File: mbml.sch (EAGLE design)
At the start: 16 parts, among them IC1 MAX392CPE, J1 CON-2B2B-XH-A(LF)(SN), J2 CON-2B2B-XH-A(LF)(SN), K1 G5SB, Q1 2N2222, X1 43160-1102

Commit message: Finished board
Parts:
- removed IC1: MAX392CPE, maxim:MAX392CPE
- removed J1, J2, U$2, U$3, U$4: CON-2B2B-XH-A(LF)(SN), FVP:CON-2B2B-XH-A(LF)(SN)
- removed U$5: CON-2, FVP:CON-2
- added OK1: ILQ1, optocoupler:ILQ1
- added R1, R2, R3, R6: 470, resistor:R-US_0204/5
- added R4, R5: 10k, resistor:R-US_0204/5
- added X2: CON-2, FVP:CON-2
- added X3, X4, X5, X6, X7, X8: CON-2B2B-XH-A(LF)(SN), FVP:CON-2B2B-XH-A(LF)(SN)
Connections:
- new net N$15: OK1A.COL, X7.1
- new net N$16: OK1A.EMIT, X7.2
- new net N$17: OK1D.A, R6.1
- new net N$18: R6.2, U$1.D9
- new net N$19: OK1D.COL, X8.1
- new net N$20: OK1D.EMIT, X8.2
- new net N$7: OK1B.A, R2.1
- net GND: now also OK1A.C, OK1B.C, OK1C.C, OK1D.C, R4.2, R5.2, X2.1, X3.1, X4.1; no longer J1.1, J2.1, U$5.1
- net MON_PWR: now also X2.2; no longer U$5.2
- net N$1: now also R4.1, X4.2; no longer J2.2
- net N$10: now also R3.2; no longer IC1.IN1
- net N$11: now also OK1C.COL, X5.1; no longer IC1.NO3, U$4.2
- net N$12: now also OK1C.EMIT, X5.2; no longer IC1.COM3, U$4.1
- net N$13: now also OK1B.COL, X6.1; no longer IC1.COM2, U$3.1
- net N$14: now also OK1B.EMIT, X6.2; no longer IC1.COM1, U$2.1
- net N$2: now also R5.1, X3.2; no longer J1.2
- net N$4: now also R1.2; no longer IC1.IN3
- net N$5: now also U$1.D10; no longer U$1.D9
- net N$6: now also OK1C.A, R3.1; no longer IC1.NO1, U$2.2
- net N$8: now also OK1A.A, R1.1; no longer IC1.NO2, U$3.2
- net N$9: now also R2.2; no longer IC1.IN2
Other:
- note added: "1.0.0"
- note added: "9-23-16"
- note added: "A"
- note added: "AUX"
- note added: "CLIENT:"
- note added: "CONNECTOR"
- note added: "CPU"
- note added: "DATE:"
- note added: "FORMAT:"
- note added: "FULL VIEW PRODUCTIONS"
- note added: "HOLES"
- note added: "MBML1 CONTROL BOARD"
- note added: "MCU"
- note added: "MONITOR"
- note added: "MONITOR POWER RELAY"
- note added: "OPTO-ISOLATED COMPONENT SWITCHING"
- note added: "POWER BUTTONS"
- note added: "POWER INPUT CONNECTOR"
- note added: "PROJ"
- note added: "PROJECT:"
- note added: "SPKR"
- note added: "TINKER TECH CONSULTING, LLC"
- note added: "VERSION:"
- moved on the sheet: D1, H1, H2, H3, H4, K1, Q1, X1-1, X1-2

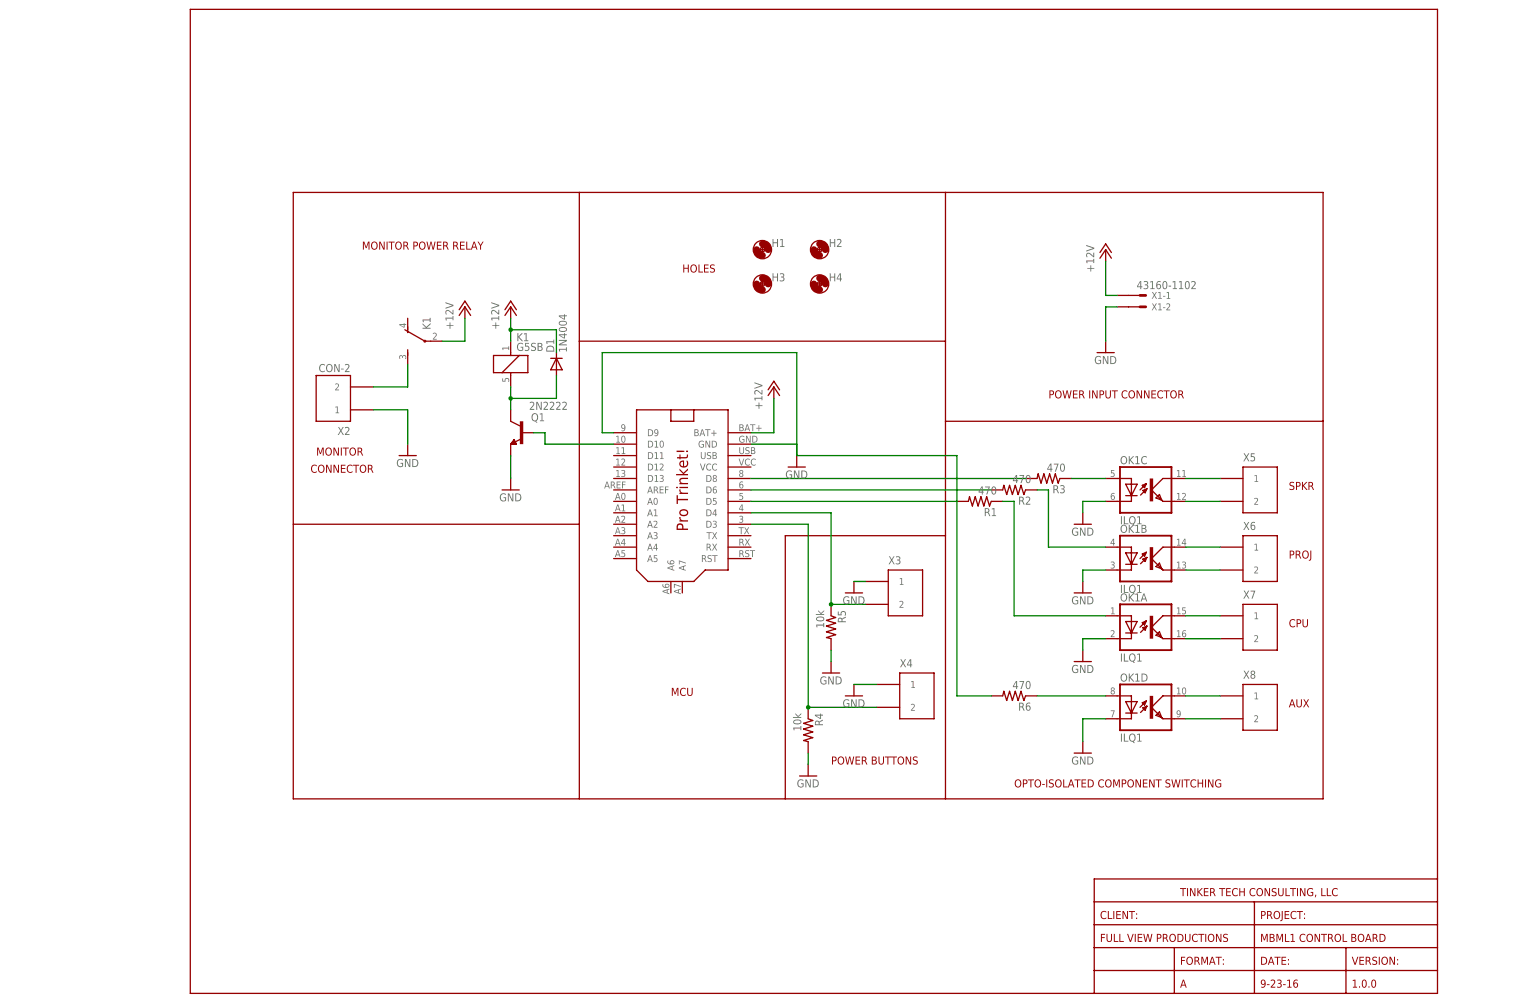
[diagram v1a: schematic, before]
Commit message: Version 2.0 Changes
Added:
- 5V regulator
- Speaker power connector
- Fan power connector
- Fan power photocoupler

Fixed:
- Missing monitor relay transistor base current limiting resistor
- Changed power button resistors from pull down to pull up
- Increased spacing between MCU pin holes to allow for installation of
female headers
- Added more GND test vias
- Added +12V and +5V test via
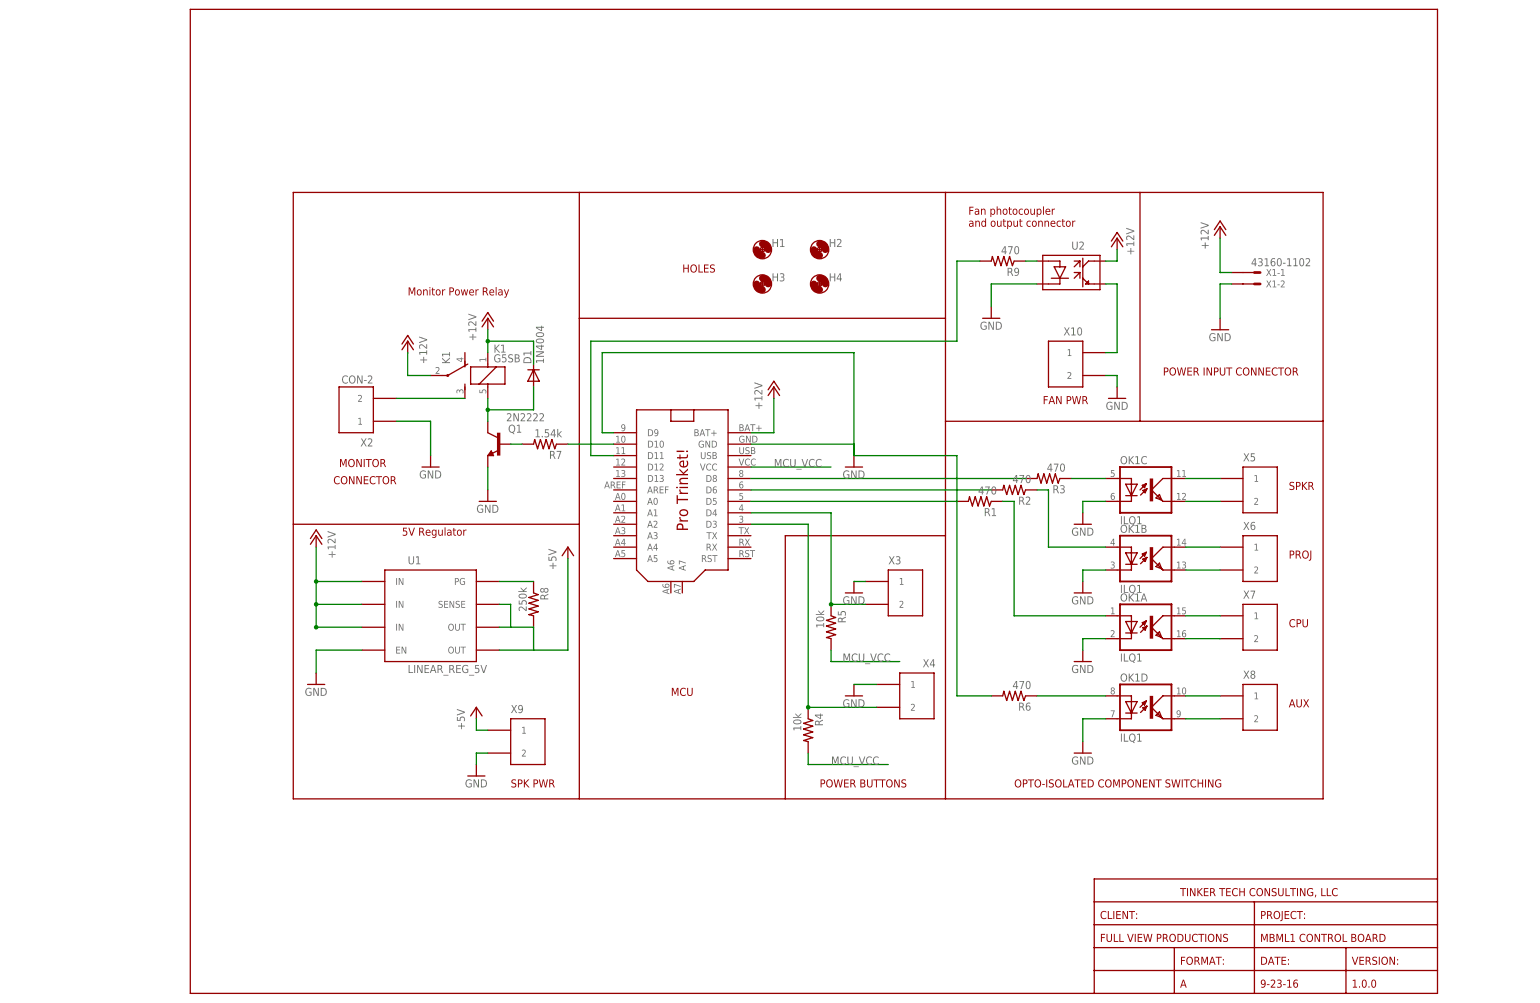
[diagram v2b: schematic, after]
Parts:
- added R7: 1.54k, resistor:R-US_0204/5
- added R8: 250k, resistor:R-US_0204/5
- added R9: 470, resistor:R-US_0204/5
- added U1: LINEAR_REG_5V, TinkerTech:LINEAR_REG_5V
- added U2: PHOTOCOUPLER, TinkerTech:PHOTOCOUPLER
- added X10, X9: CON-2B2B-XH-A(LF)(SN), FVP:CON-2B2B-XH-A(LF)(SN)
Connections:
- new net +5V: R8.2, U1.OUT@1, U1.OUT@2, U1.SENSE, X9.1
- new net MCU_VCC: R4.2, R5.2, U$1.VCC
- new net N$35: R7.1, U$1.D10
- new net N$46: R9.1, U2.P$1
- new net N$47: R9.2, U$1.D11
- new net N$48: R8.1, U1.PG
- new net N$49: U2.P$3, X10.1
- net +12V: now also U1.IN@1, U1.IN@2, U1.IN@3, U2.P$4
- net GND: now also U1.EN, U2.P$2, X10.2, X9.2; no longer R4.2, R5.2
- net N$5: now also R7.2; no longer U$1.D10
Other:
- note added: "5V Regulator"
- note added: "FAN PWR"
- note added: "Fan photocoupler and output connector"
- note added: "Monitor Power Relay"
- note added: "SPK PWR"
- note removed: "MONITOR POWER RELAY"
- moved on the sheet: D1, K1, Q1, X1-1, X1-2, X2

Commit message: Starting major overhaul
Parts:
- removed R9: 470, resistor:R-US_0204/5
- removed U2: PHOTOCOUPLER, TinkerTech:PHOTOCOUPLER
- added C1: (no value), SparkFun-Passives:CAPPTH
- added C2: (no value), TinkerTech:CAP_POL
- R7: value 1.54k -> 1.5k
- X10: value CON-2B2B-XH-A(LF)(SN) -> CON_DB9VERT; device FVP:CON-2B2B-XH-A(LF)(SN) -> TinkerTech:CON_DB9VERT
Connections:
- net N$1 renamed D3
- net N$10 renamed D8
- net N$18 renamed D9
- net N$2 renamed D4
- net N$3 renamed TRANS_COLLECTOR
- net N$35 renamed D10
- net N$4 renamed D5
- net N$5 renamed TRANS_BASE
- net N$9 renamed D6
- removed net N$13: OK1B.COL, X6.1
- removed net N$46: R9.1, U2.P$1
- removed net N$47: R9.2, U$1.D11
- removed net N$49: U2.P$3, X10.1
- new net A0: U$1.A0
- new net A1: U$1.A1
- new net A2: U$1.A2
- new net A3: U$1.A3
- new net A4: U$1.A4
- new net A5: U$1.A5
- new net A6: U$1.A6
- new net A7: U$1.A7
- new net AREF: U$1.AREF
- new net D11: U$1.D11
- new net D12: U$1.D12
- new net D13: U$1.D13
- new net RST: U$1.RST
- new net RX: U$1.RX, X10.RX
- new net TX: U$1.TX, X10.TX
- new net USB: U$1.USB
- net +12V: now also C1.1, OK1B.COL; no longer U2.P$4
- net +5V: now also C2.+
- net GND: now also C1.2, C2.-, X10.GND, X6.2; no longer U2.P$2, X10.2
- net N$14: now also X6.1; no longer X6.2
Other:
- note removed: "Fan photocoupler and output connector"
- note removed: "PROJ"
- moved on the sheet: OK1A, OK1B, OK1D, R6, X6, X7, X8, X9

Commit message: Ready for production
Hopefully…
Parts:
- removed X5, X8, X9: CON-2B2B-XH-A(LF)(SN), FVP:CON-2B2B-XH-A(LF)(SN)
- added D2: (no value), TinkerTech:DIODE
- added L1: (no value), TinkerTech:INDUCTORRADIAL_8.5-DIA_5-SPACE
- added MAIN_LED, PROJ_LED, SPKR_PWR, SPKR_SW, SPRK_SENSE: CON-2B2B-XH-A(LF)(SN), FVP:CON-2B2B-XH-A(LF)(SN)
- added R10, R9: 470, resistor:R-US_0204/5
- C1: value (none) -> 100uF; device SparkFun-Passives:CAPPTH -> TinkerTech:CAP_POL6.3-DIA_2.5-SPACE
- C2: value (none) -> 330uF; device TinkerTech:CAP_POL -> TinkerTech:CAP_POL10-DIA_5-SPACE
- R3: value 470 -> 10k
- R8: value 250k -> 470
- U1: value LINEAR_REG_5V -> REG_5V_SWITCHING_SI-8050E; device TinkerTech:LINEAR_REG_5V -> TinkerTech:REG_5V_SWITCHING_SI-8050E
- renumbered X3 to MAIN_PWR, X4 to PROJ_PWR, X6 to FAN_PWR, X7 to CPU_SW
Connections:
- removed net D8: R3.2, U$1.D8
- removed net N$12: OK1C.EMIT, X5.2
- removed net N$19: OK1D.COL, X8.1
- removed net N$20: OK1D.EMIT, X8.2
- removed net N$48: R8.1, U1.PG
- new net AUX_1: OK1D.COL
- new net AUX_2: OK1D.EMIT
- new net N$1: D2.-, L1.P$1, U1.SW_OUT
- new net N$2: OK1C.A, R8.1
- new net N$3: R8.2, U$1.D8
- new net N$4: OK1C.COL, SPKR_SW.1
- new net N$5: OK1C.EMIT, SPKR_SW.2
- net +12V: now also C1.+, U1.IN; no longer C1.1, U1.IN@1, U1.IN@2, U1.IN@3
- net +5V: now also L1.P$2, SPKR_PWR.1, U1.V_OS; no longer R8.2, U1.OUT@1, U1.OUT@2, U1.SENSE, X9.1
- net D11: now also R3.2, SPRK_SENSE.1
- net D12: now also R10.2
- net D13: now also R9.2
- net GND: now also C1.-, D2.+, MAIN_LED.2, PROJ_LED.2, SPKR_PWR.2, SPRK_SENSE.2, U1.GND; no longer C1.2, U1.EN, X9.2
- net MCU_VCC: now also R3.1
- net N$11: now also MAIN_LED.1, R10.1; no longer OK1C.COL, X5.1
- net N$6: now also PROJ_LED.1, R9.1; no longer OK1C.A, R3.1
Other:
- note removed: "AUX"
- note removed: "CPU"
- note removed: "FAN PWR"
- note removed: "SPK PWR"
- note removed: "SPKR"
- moved on the sheet: H1, H2, H3, H4, R3, R8

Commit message: Version 2.1, DRC OK
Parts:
- removed H3: MOUNT-HOLE3.0, holes:MOUNT-HOLE3.0
- removed X10: CON_DB9VERT, TinkerTech:CON_DB9VERT
- added AUX_1, AUX_2, PROJ_BLANK: CON-2B2B-XH-A(LF)(SN), FVP:CON-2B2B-XH-A(LF)(SN)
- added D3: 1N4004, diode:1N4004
- added K2: 68800611622, Wurth_Wire_to_Board_Connectors_rev15d:68800611622
- added Q2: IRLZ24LPBF, transistor-power:PMOSFET_N
- added R11: 100, resistor:R-US_0204/5
- added R12, R13: 10k, resistor:R-US_0204/5
- R9: value 470 -> 1.8k
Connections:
- removed net AUX_1: OK1D.COL
- removed net AUX_2: OK1D.EMIT
- new net N$10: Q2.G, R11.1, R12.1
- new net N$12: AUX_1.2, OK1B.COL
- new net N$13: AUX_1.1, OK1B.EMIT
- new net N$18: CPU_SW.1, OK1D.EMIT
- new net N$9: D3.A, FAN_PWR.2, Q2.D
- net +12V: now also D3.C, FAN_PWR.1; no longer OK1B.COL
- net A3: now also PROJ_BLANK.2, R13.1
- net A4: now also R11.2
- net GND: now also K2.5, PROJ_BLANK.1, Q2.S, R12.2; no longer FAN_PWR.2, X10.GND
- net MCU_VCC: now also K2.6, R13.2
- net N$14: now also CPU_SW.2, OK1D.COL; no longer FAN_PWR.1, OK1B.EMIT
- net N$15: now also AUX_2.1; no longer CPU_SW.1
- net N$16: now also AUX_2.2; no longer CPU_SW.2
- net RX: now also K2.4; no longer X10.RX
- net TX: now also K2.3; no longer X10.TX
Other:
- moved on the sheet: C1, C2, CPU_SW, D1, D2, FAN_PWR, H1, H2, H4, K1, L1, MAIN_LED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

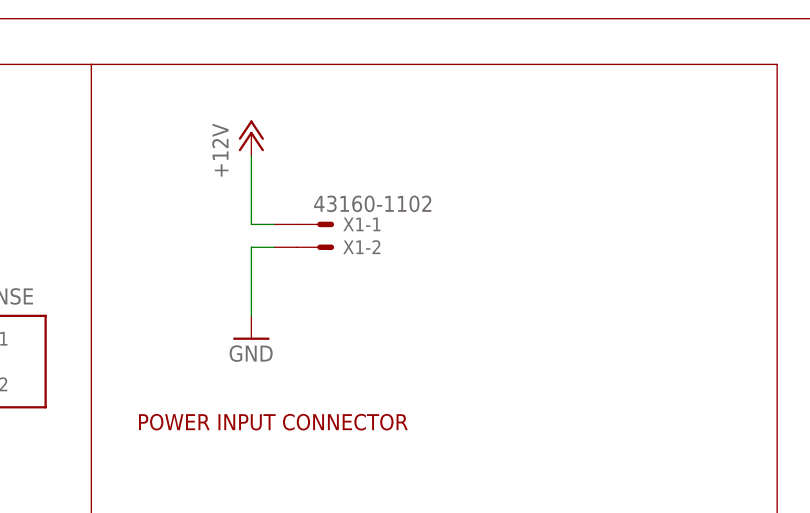
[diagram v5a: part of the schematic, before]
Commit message: Added reverse polarity protection
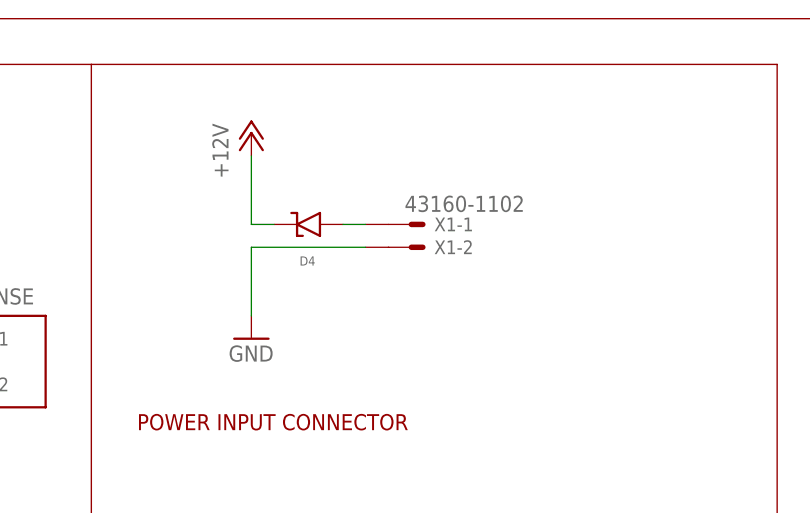
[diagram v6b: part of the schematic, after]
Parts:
- added D4: (no value), TinkerTech:DIODE_SHOTTKY
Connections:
- new net +12V_IN: D4.+, X1-1.S@1
- net +12V: now also D4.-; no longer X1-1.S@1
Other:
- moved on the sheet: X1-1, X1-2
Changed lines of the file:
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@@
 <part name="AUX_1" library="FVP" deviceset="CON-2" device="B2B-XH-A(LF)(SN)"/>
 <part name="CPU_SW" library="FVP" deviceset="CON-2" device="B2B-XH-A(LF)(SN)"/>
+<part name="D4" library="TinkerTech" deviceset="DIODE_SHOTTKY" device=""/>
 </parts>
 <sheets>
@@
 <attribute name="NAME" x="215.9" y="118.11" size="1.778" layer="95"/>
 </instance>
-<instance part="X1" gate="-1" x="218.44" y="195.58"/>
-<instance part="X1" gate="-2" x="218.44" y="193.04"/>
+<instance part="X1" gate="-1" x="228.6" y="195.58"/>
+<instance part="X1" gate="-2" x="228.6" y="193.04"/>
 <instance part="P+3" gate="1" x="210.82" y="205.74"/>
 <instance part="GND4" gate="1" x="210.82" y="182.88"/>
@@
 <attribute name="NAME" x="215.9" y="102.87" size="1.778" layer="95" rot="MR180"/>
 </instance>
+<instance part="D4" gate="G$1" x="215.9" y="195.58" rot="R180"/>
 </instances>
 <busses>
@@
 <segment>
 <pinref part="X1" gate="-2" pin="S@1"/>
-<wire x1="213.36" y1="193.04" x2="210.82" y2="193.04" width="0.1524" layer="91"/>
+<wire x1="223.52" y1="193.04" x2="210.82" y2="193.04" width="0.1524" layer="91"/>
 <wire x1="210.82" y1="193.04" x2="210.82" y2="185.42" width="0.1524" layer="91"/>
 <pinref part="GND4" gate="1" pin="GND"/>
@@
 </segment>
 <segment>
-<pinref part="X1" gate="-1" pin="S@1"/>
-<wire x1="213.36" y1="195.58" x2="210.82" y2="195.58" width="0.1524" layer="91"/>
 <wire x1="210.82" y1="195.58" x2="210.82" y2="203.2" width="0.1524" layer="91"/>
 <pinref part="P+3" gate="1" pin="+12V"/>
+<pinref part="D4" gate="G$1" pin="-"/>
+<wire x1="210.82" y1="195.58" x2="213.36" y2="195.58" width="0.1524" layer="91"/>
 </segment>
 <segment>
@@
 </segment>
 </net>
+<net name="+12V_IN" class="0">
+<segment>
+<pinref part="D4" gate="G$1" pin="+"/>
+<pinref part="X1" gate="-1" pin="S@1"/>
+<wire x1="220.98" y1="195.58" x2="223.52" y2="195.58" width="0.1524" layer="91"/>
+</segment>
+</net>
